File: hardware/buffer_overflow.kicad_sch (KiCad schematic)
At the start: 34 parts, among them J1 In, J2 Out, J3 +, J4 FS, J5 In_G, J6 Out_G, J7 -, J8 FS_G, U1 LM741

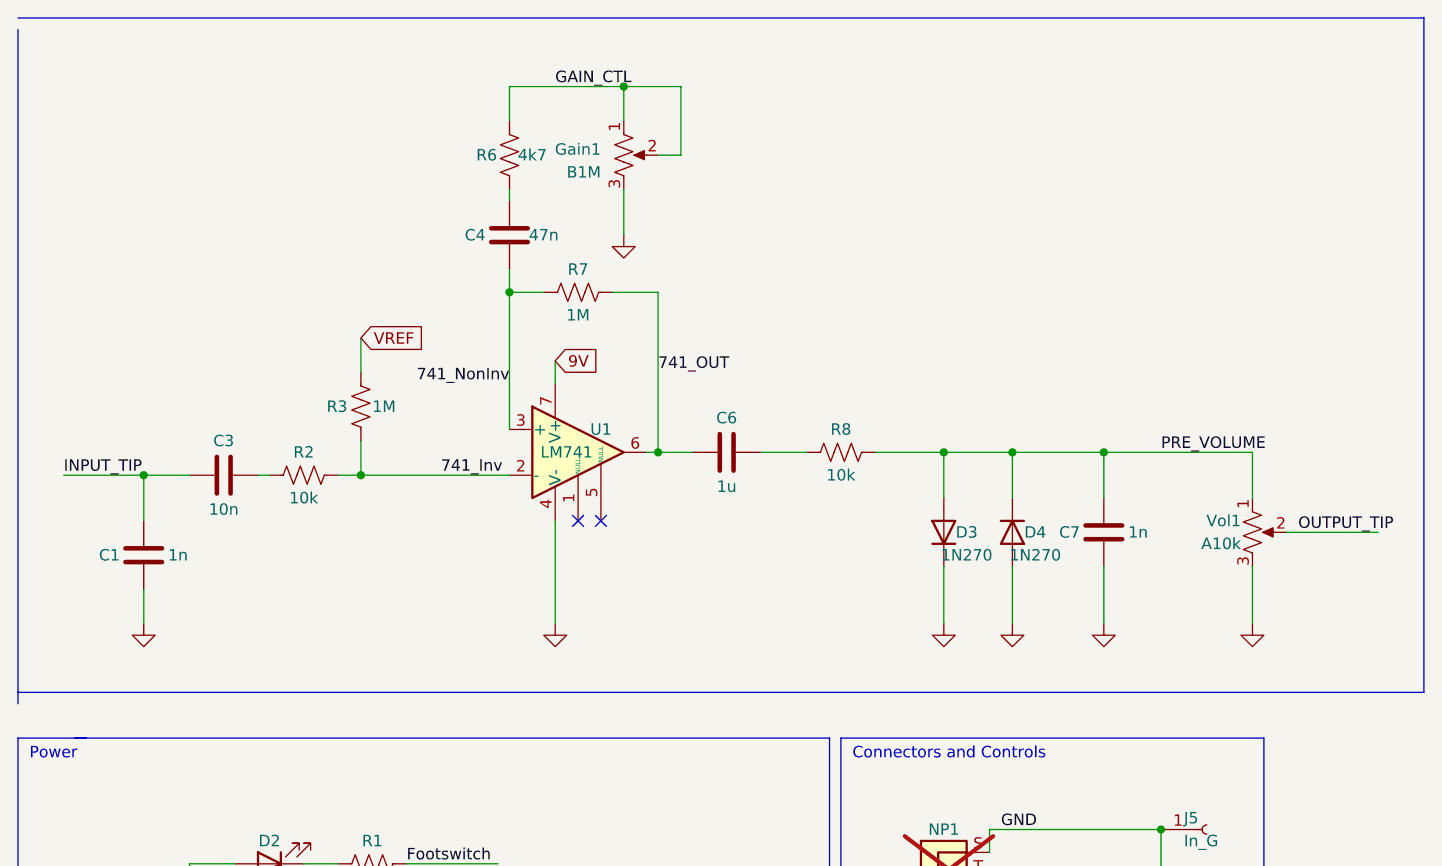
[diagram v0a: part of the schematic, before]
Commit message: Fix issues identified in v0.01
Bugfixes:
 - Reverse swapped opamp inputs
 - Reverse backwards Volume potentiometer

Enhancements:
 - Cosmetic and functional updates to silkscreen
 - Include revision and github reference
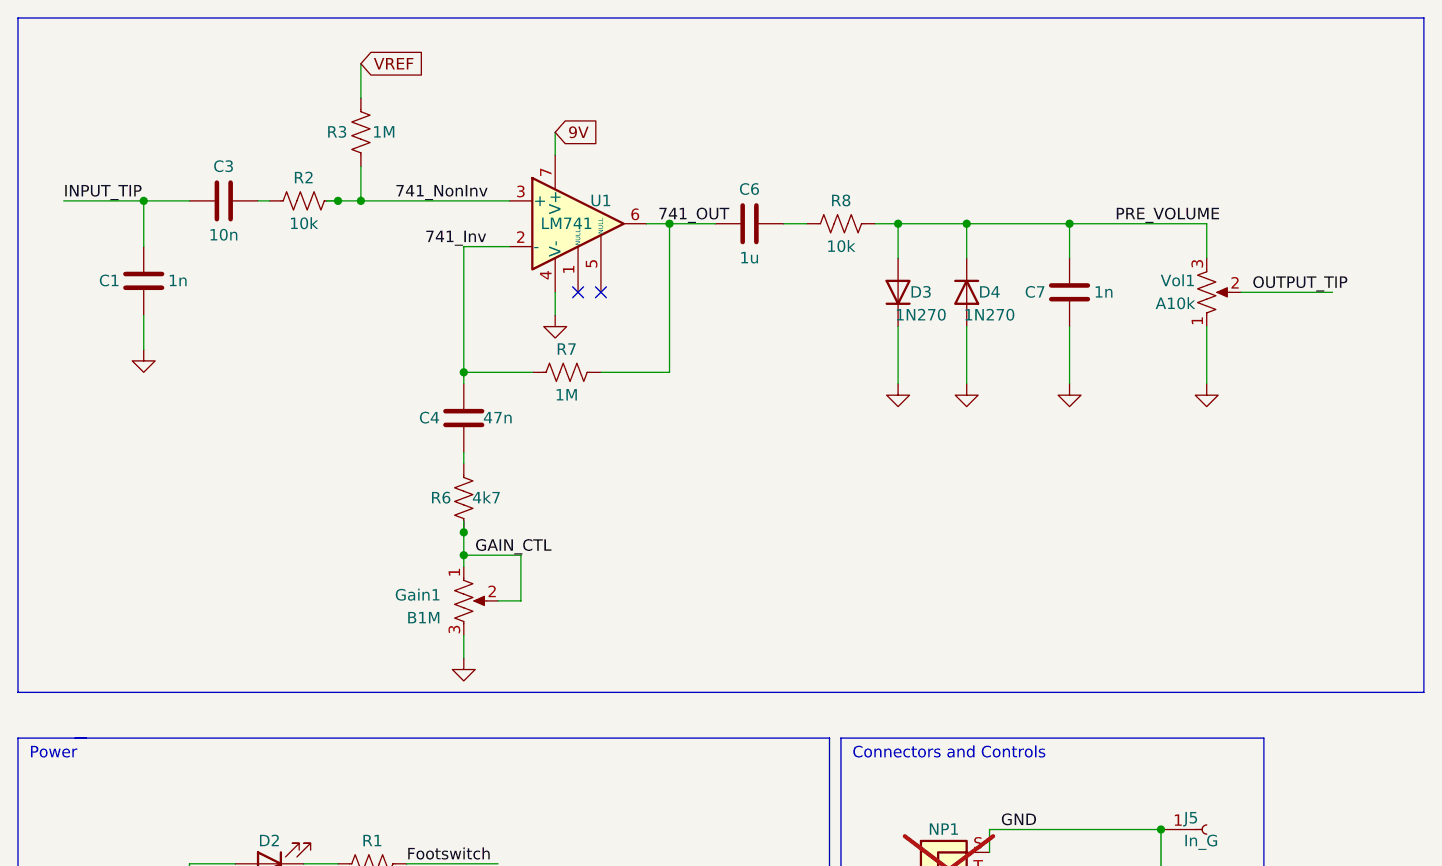
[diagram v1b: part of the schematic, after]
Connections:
- net 741_Inv: now also C4.2, R7.2; no longer R2.2, R3.1
- net 741_NonInv: now also R2.2, R3.1; no longer C4.1, R7.2
- net GAIN_CTL: now also R6.2; no longer R6.1
- net GND: now also Vol1.1; no longer Vol1.3
- net PRE_VOLUME: now also Vol1.3; no longer Vol1.1
- new net: C4.1, R6.1
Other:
- moved on the sheet: C1, C3, C4, C6, C7, D3, D4, Gain1, R2, R3, R6, R7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

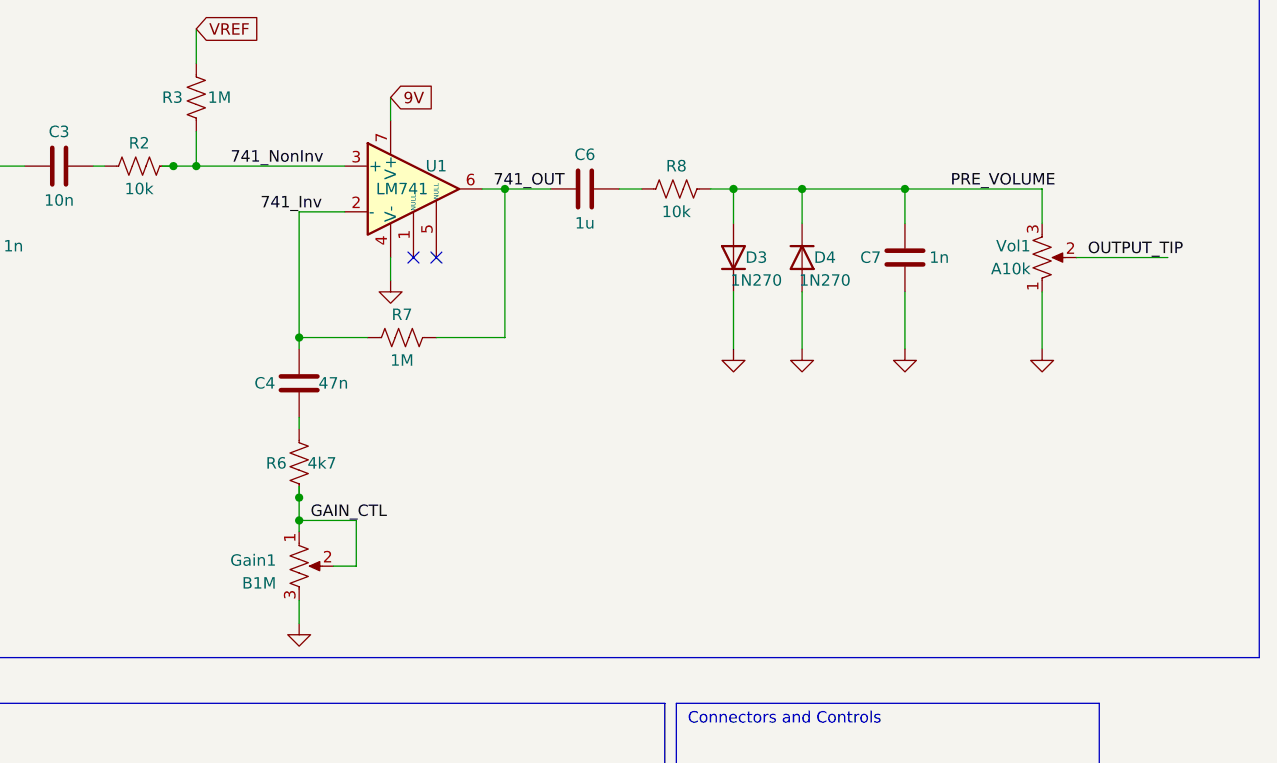
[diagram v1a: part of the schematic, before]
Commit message: Mostly cosmetic updates
 - replace LED footprint with 3mm non-flat
 - shift text around
 - fix grid alignment for edge cuts
 - misc text updates
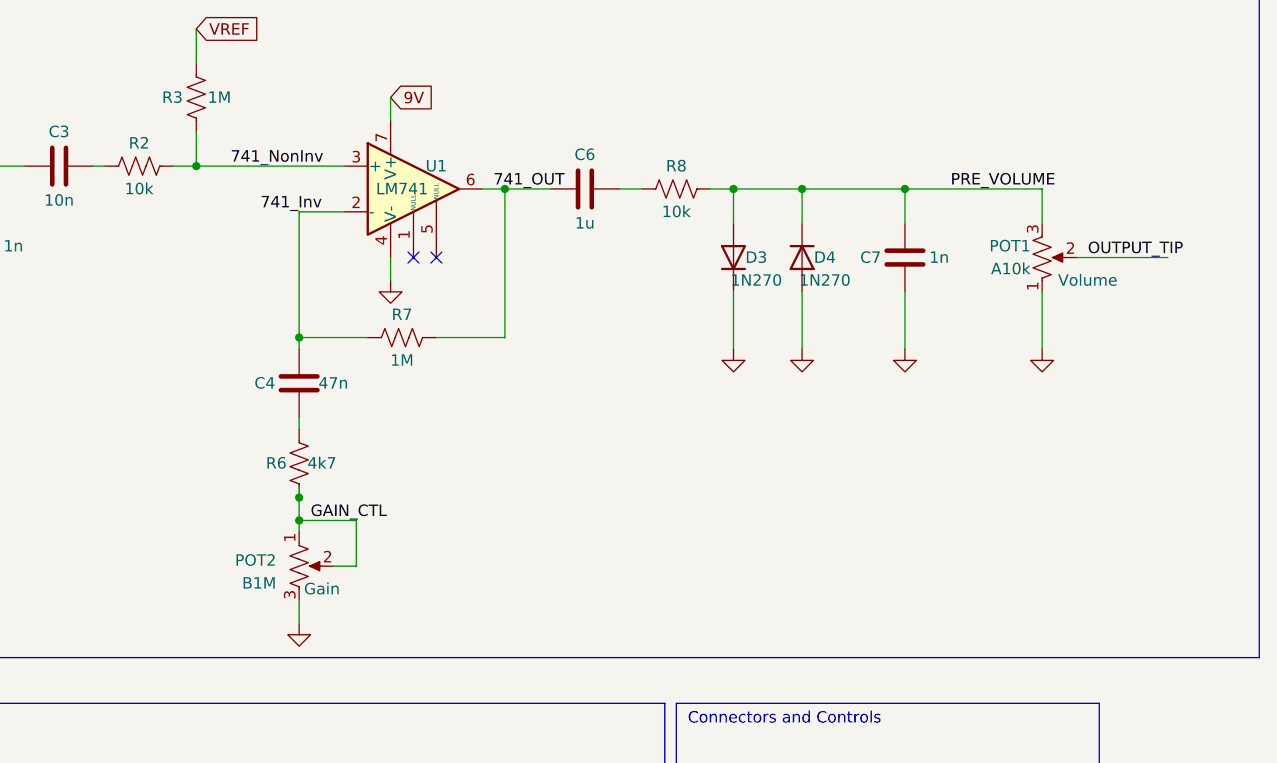
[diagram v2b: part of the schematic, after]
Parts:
- D2: footprint LED_THT:LED_D5.0mm_FlatTop -> LED_THT:LED_D3.0mm
- POT1: renamed from Vol1; Label (none) -> Volume
- POT2: renamed from Gain1; Label (none) -> Gain
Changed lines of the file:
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@@
   (title_block
     (title "Buffer Overflow Drive Effect")
-    (date "2023-02-14")
-    (rev "0.1")
+    (date "2023-02-22")
+    (rev "v0.2")
   )
   (junction (at 81.28 149.86) (diameter 0) (color 0 0 0 0)
@@
   )
   (junction (at 81.28 137.16) (diameter 0) (color 0 0 0 0)
-  )
-  (junction (at 50.8 35.56) (diameter 0) (color 0 0 0 0)
   )
   (junction (at 53.34 35.56) (diameter 0) (color 0 0 0 0)
@@
   )
   (wire (pts (xy 123.19 129.54) (xy 123.19 127))
-    (stroke (width 0) (type default))
-  )
-  (wire (pts (xy 49.53 35.56) (xy 50.8 35.56))
     (stroke (width 0) (type default))
   )
@@
       (effects (font (size 1.27 1.27)))
     )
-    (property "Footprint" "LED_THT:LED_D5.0mm_FlatTop" (at 43.18 109.22 0)
+    (property "Footprint" "LED_THT:LED_D3.0mm" (at 43.18 109.22 0)
       (effects (font (size 1.27 1.27)) hide)
     )
@@
   (symbol (lib_id "Device:R_Potentiometer_US") (at 147.32 45.72 0) (mirror x) (unit 1)
     (in_bom yes) (on_board yes) (dnp no)
-    (property "Reference" "Vol1" (at 146.05 44.45 0)
+    (property "Reference" "POT1" (at 146.05 44.45 0)
       (effects (font (size 1.27 1.27)) (justify right))
     )
@@
       (effects (font (size 1.27 1.27)) hide)
     )
+    (property "Label" "Volume" (at 152.4 48.26 0)
+      (effects (font (size 1.27 1.27)))
+    )
     (pin "1")
     (pin "2")
@@
       (project "buffer_overflow"
         (path "/65eca179-3106-4a88-bde8-4fcb23cd7118"
-          (reference "Vol1") (unit 1)
+          (reference "POT1") (unit 1)
         )
       )
@@
   )
   (symbol (lib_id "Device:R_Potentiometer_US") (at 64.77 80.01 0) (unit 1)
-    (in_bom yes) (on_board yes) (dnp no) (fields_autoplaced)
-    (property "Reference" "Gain1" (at 62.23 79.3749 0)
+    (in_bom yes) (on_board yes) (dnp no)
+    (property "Reference" "POT2" (at 62.23 79.3749 0)
       (effects (font (size 1.27 1.27)) (justify right))
     )
@@
       (effects (font (size 1.27 1.27)) hide)
     )
+    (property "Label" "Gain" (at 67.31 82.55 0)
+      (effects (font (size 1.27 1.27)))
+    )
     (pin "1")
     (pin "2")
@@
       (project "buffer_overflow"
         (path "/65eca179-3106-4a88-bde8-4fcb23cd7118"
-          (reference "Gain1") (unit 1)
-        )
-      )
+          (reference "POT2") (unit 1)
+        )
+      )

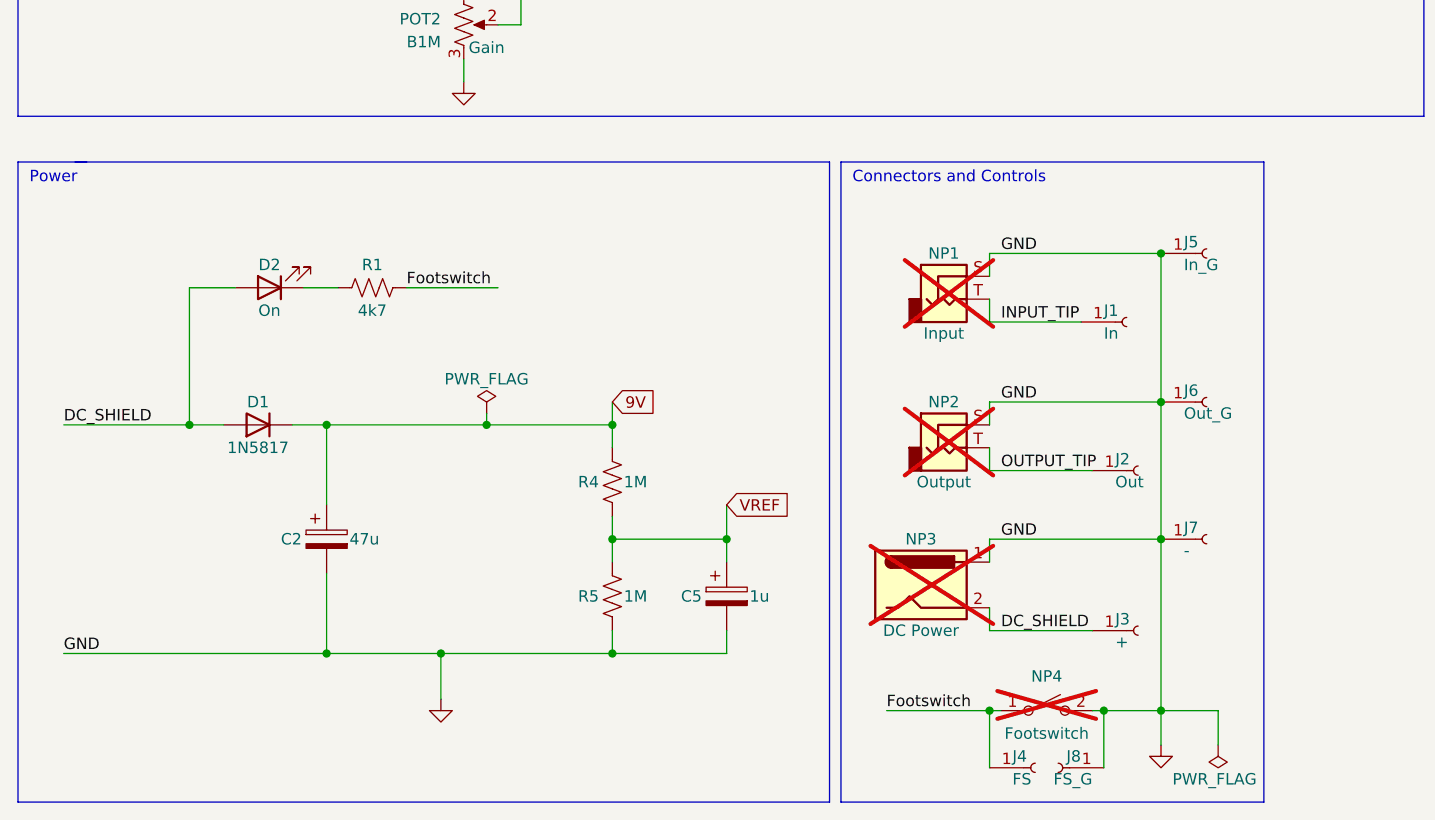
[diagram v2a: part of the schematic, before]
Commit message: Updates for v0.30:  - Replace wire connections with molex picoblade connectors  - Many cosmetic changes and layout changes to reduce size and improve appearance
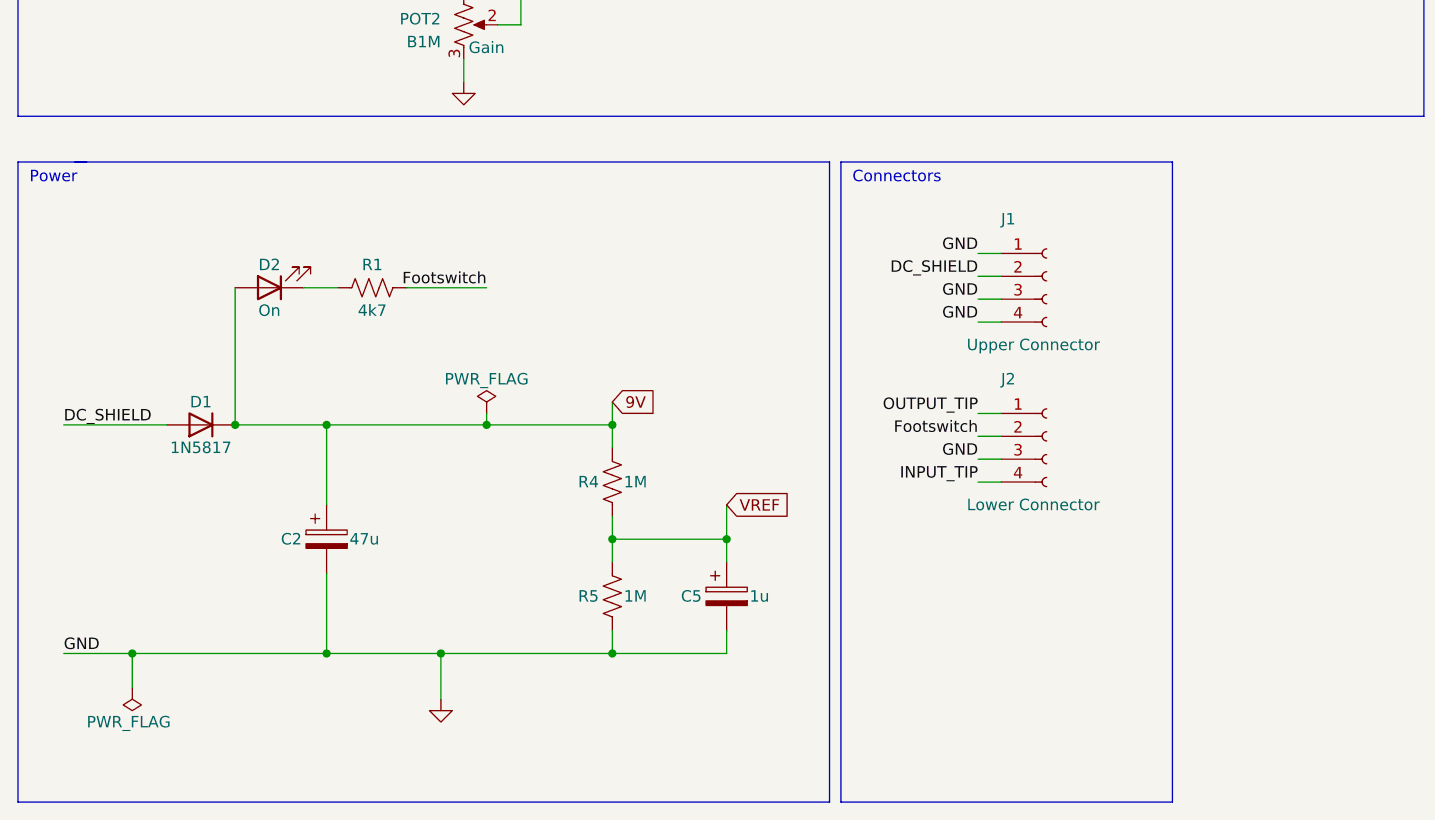
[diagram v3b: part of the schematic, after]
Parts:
- removed J1: In, Connector_Wire:SolderWire-0.5sqmm_1x01_D0.9mm_OD2.1mm, symbol Connector:Conn_01x01_Socket
- removed J2: Out, Connector_Wire:SolderWire-0.5sqmm_1x01_D0.9mm_OD2.1mm, symbol Connector:Conn_01x01_Socket
- removed J3: +, Connector_Wire:SolderWire-0.5sqmm_1x01_D0.9mm_OD2.1mm, symbol Connector:Conn_01x01_Socket
- removed J4: FS, Connector_Wire:SolderWire-0.5sqmm_1x01_D0.9mm_OD2.1mm, symbol Connector:Conn_01x01_Socket
- removed J5: In_G, Connector_Wire:SolderWire-0.5sqmm_1x01_D0.9mm_OD2.1mm, symbol Connector:Conn_01x01_Socket
- removed J6: Out_G, Connector_Wire:SolderWire-0.5sqmm_1x01_D0.9mm_OD2.1mm, symbol Connector:Conn_01x01_Socket
- removed J7: -, Connector_Wire:SolderWire-0.5sqmm_1x01_D0.9mm_OD2.1mm, symbol Connector:Conn_01x01_Socket
- removed J8: FS_G, Connector_Wire:SolderWire-0.5sqmm_1x01_D0.9mm_OD2.1mm, symbol Connector:Conn_01x01_Socket
- removed NP1: Input, symbol Connector_Audio:AudioJack2
- removed NP2: Output, symbol Connector_Audio:AudioJack2
- removed NP3: DC Power, symbol Connector:Jack-DC
- removed NP4: Footswitch, Connector_Pin:Pin_D1.0mm_L10.0mm, symbol Switch:SW_SPST
- added J1: Upper Connector, Connector_Molex:Molex_PicoBlade_53047-0410_1x04_P1.25mm_Vertical, symbol Connector:Conn_01x04_Socket
- added J2: Lower Connector, Connector_Molex:Molex_PicoBlade_53047-0410_1x04_P1.25mm_Vertical, symbol Connector:Conn_01x04_Socket
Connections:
- net 9V: now also D2.2 (A)
- net DC_SHIELD: now also J1.2 (Pin_2); no longer D2.2 (A)
- net Footswitch: now also J2.2 (Pin_2)
- net GND: now also J1.1 (Pin_1), J1.3 (Pin_3), J1.4 (Pin_4), J2.3 (Pin_3)
- net INPUT_TIP: now also J2.4 (Pin_4)
- net OUTPUT_TIP: now also J2.1 (Pin_1)
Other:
- note added: "Connectors"
- note removed: "Connectors and Controls"
- company: (none) -> github.com/whbeers/buffer_overflow
- moved on the sheet: D1
